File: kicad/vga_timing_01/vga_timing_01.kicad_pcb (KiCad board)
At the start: 2 copper layers, 45.7 x 45.7 mm, 10 parts, among them J1 Conn_02x01, U1 74LS393, U2 74LS393, U3 74LS393, U4 PAL20RS10, U5 PAL20RS10, X1 ACO-14MHz

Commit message: vga timing board 01 work
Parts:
- moved U3 45.4 mm to (121.4, 53.3)
- moved C3 42.8 mm to (114.8, 50.8)
- moved J1 37.7 mm to (64.4, 48.5)
- moved X1 33.8 mm to (63.5, 58.9), turned to 90 degrees
- moved C4 26.2 mm to (100.3, 50.8), turned to 180 degrees
- moved U2 23.1 mm to (106.9, 53.3)
- moved U1 15.4 mm to (92.5, 53.3)
- moved C5 7.45 mm to (85.9, 50.8)
- moved U5 5.92 mm to (96.5, 45.7), turned to 90 degrees
- moved U4 5.68 mm to (63.5, 45.7), turned to 90 degrees
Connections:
- U1 pad 1: /H03 -> /CLOCK
- U1 pad 10: /V05 -> /H05
- U1 pad 11: /V04 -> /H04
- U1 pad 12: /~{V_RES} -> /~{H_RES}
- U1 pad 13: /V03 -> /H03
- U1 pad 3: /H04 -> /H00
- U1 pad 4: /H05 -> /H01
- U1 pad 5: /H06 -> /H02
- U1 pad 6: /H07 -> /H03
- U1 pad 8: /V07 -> /H07
- U1 pad 9: /V06 -> /H06
- U2 pad 1: /CLOCK -> /H07
- U2 pad 3: /H00 -> /H08
- U2 pad 4: /H01 -> /H09
- U2 pad 5: /H02 -> /H10
- U2 pad 6: /H03 -> /H11
- U3 pad 1: /H07 -> /V03
- U3 pad 2: /~{H_RES} -> /~{V_RES}
- U3 pad 3: /H08 -> /V04
- U3 pad 4: /H09 -> /V05
- U3 pad 5: /H10 -> /V06
- U3 pad 6: /H11 -> /V07
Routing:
- net /CLOCK: track 48.7 -> 66.8 mm, vias 0 -> 1
- net VCC: track 119.3 -> 135.5 mm, vias 0 -> 4
- net /~{V_RES}: track 66.4 -> 50.3 mm, vias 0 -> 1
- net /V07: track 27.1 -> 14.2 mm
- net /~{H_RES}: track 62.0 -> 73.8 mm, vias 0 -> 1
- net /H00: track 19.1 -> 29.9 mm
- net /V03: track 27.2 -> 17.9 mm
- net /H07: track 33.9 -> 24.8 mm
- net /H01: track 21.5 -> 28.2 mm
- net /V05: track 11.3 -> 17.8 mm
- net /H06: track 23.0 -> 16.7 mm
- net /V04: track 11.9 -> 18.1 mm
- net /V08: track 11.4 -> 5.99 mm
- net /V02: track 13.7 -> 8.99 mm
- net /V09: track 10.0 -> 5.46 mm
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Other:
- board size 45.7 x 45.7 mm -> 68.8 x 26.9 mm

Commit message: test kicad busses
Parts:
- moved J1 22.2 mm to (84.2, 58.4)
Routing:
- net GND: track 5.52 -> 194.8 mm, vias 6 -> 15
- net VCC: track 135.5 -> 150.3 mm
- net /CLOCK: track 66.8 -> 64.3 mm
- net /~{H_RES}: track 73.8 -> 74.4 mm
- net /~{V_RES}: track 50.3 -> 50.8 mm

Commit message: routing improvements
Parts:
- U1, U2, U3: footprint Package_SO:SOIC-14_3.9x8.7mm_P1.27mm -> Package_SO:SO-14_3.9x8.65mm_P1.27mm
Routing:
- net VCC: track 150.3 -> 141.0 mm, vias 4 -> 0
- net /H03: track 31.8 -> 29.1 mm
- net /~{H_RES}: track 74.4 -> 76.3 mm, vias 1 -> 4
- net /~{V_RES}: track 50.8 -> 52.3 mm, vias 1 -> 2
- net /CLOCK: track 64.3 -> 65.0 mm, vias 1 -> 0
- net /H09: track 25.0 -> 25.6 mm
- net GND: track 194.8 -> 195.4 mm

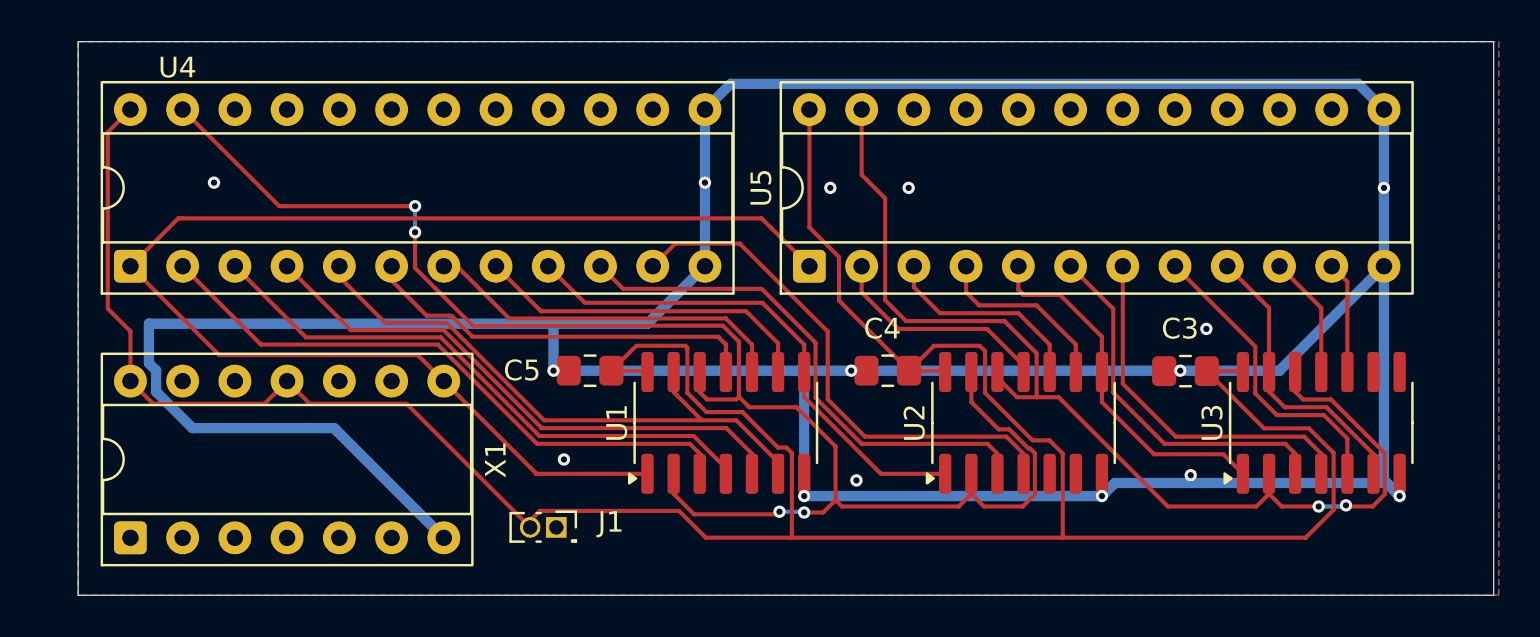
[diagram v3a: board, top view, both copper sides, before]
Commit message: WIP vga timing
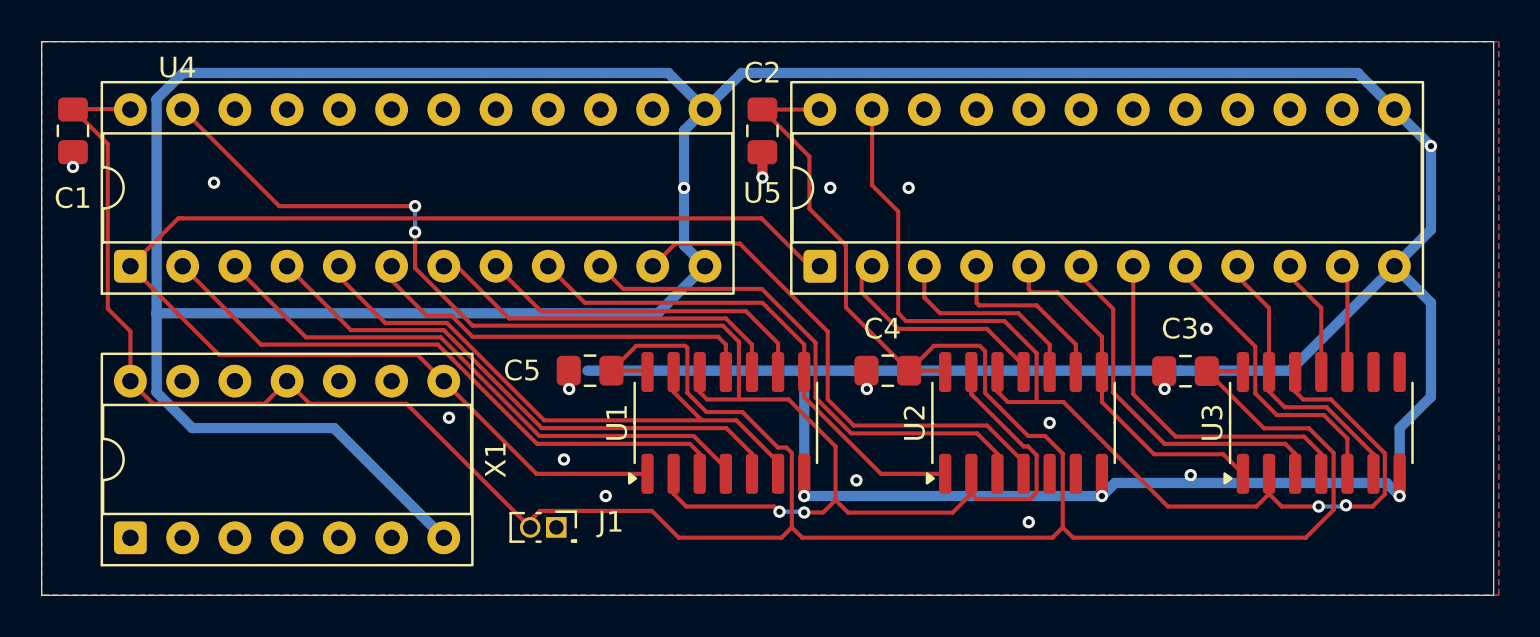
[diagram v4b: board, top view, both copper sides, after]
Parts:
- added C1: 100nF, Capacitor_SMD:C_0805_2012Metric_Pad1.18x1.45mm_HandSolder, F.Cu at (60.7, 39.1)
- added C2: 100nF, Capacitor_SMD:C_0805_2012Metric_Pad1.18x1.45mm_HandSolder, F.Cu at (94.2, 39.1)
- moved U5 0.51 mm to (97.0, 45.7)
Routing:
- net GND: track 195.4 -> 236.7 mm, vias 15 -> 21
- net VCC: track 141.0 -> 147.1 mm
- net /V03: track 17.6 -> 17.1 mm
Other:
- board size 68.8 x 26.9 mm -> 70.6 x 26.9 mm
